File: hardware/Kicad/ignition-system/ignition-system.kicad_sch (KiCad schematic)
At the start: 27 parts, among them J1 Screw_Terminal_01x02, SW1 SW_Push, SW2 SW_SPDT

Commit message: fix: socket ra02 con gnd de bordes y ntc al temp
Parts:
- added TH1: NTC 10k B3950, Connector_JST:JST_PH_S2B-PH-K_1x02_P2.00mm_Horizontal, symbol Device:Thermistor_NTC
- SW1: footprint Connector_PinHeader_2.54mm:PinHeader_1x02_P2.54mm_Vertical -> Connector_JST:JST_PH_S2B-PH-K_1x02_P2.00mm_Horizontal
- renumbered LORA2-Sx1278 to LORA-Sx1278(A)1, LORA1-Sx1278 to LORA-Sx1278(B)1
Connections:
- net GND: now also LORA-Sx1278(A)1.1 (Pin_1), LORA-Sx1278(B)1.1 (Pin_1), LORA-Sx1278(B)1.8 (Pin_8), TH1.2; no longer ModuloDeCarga1.1 (TEMP)
- new net: ModuloDeCarga1.1 (TEMP), TH1.1
- no-connect marks 24 -> 21

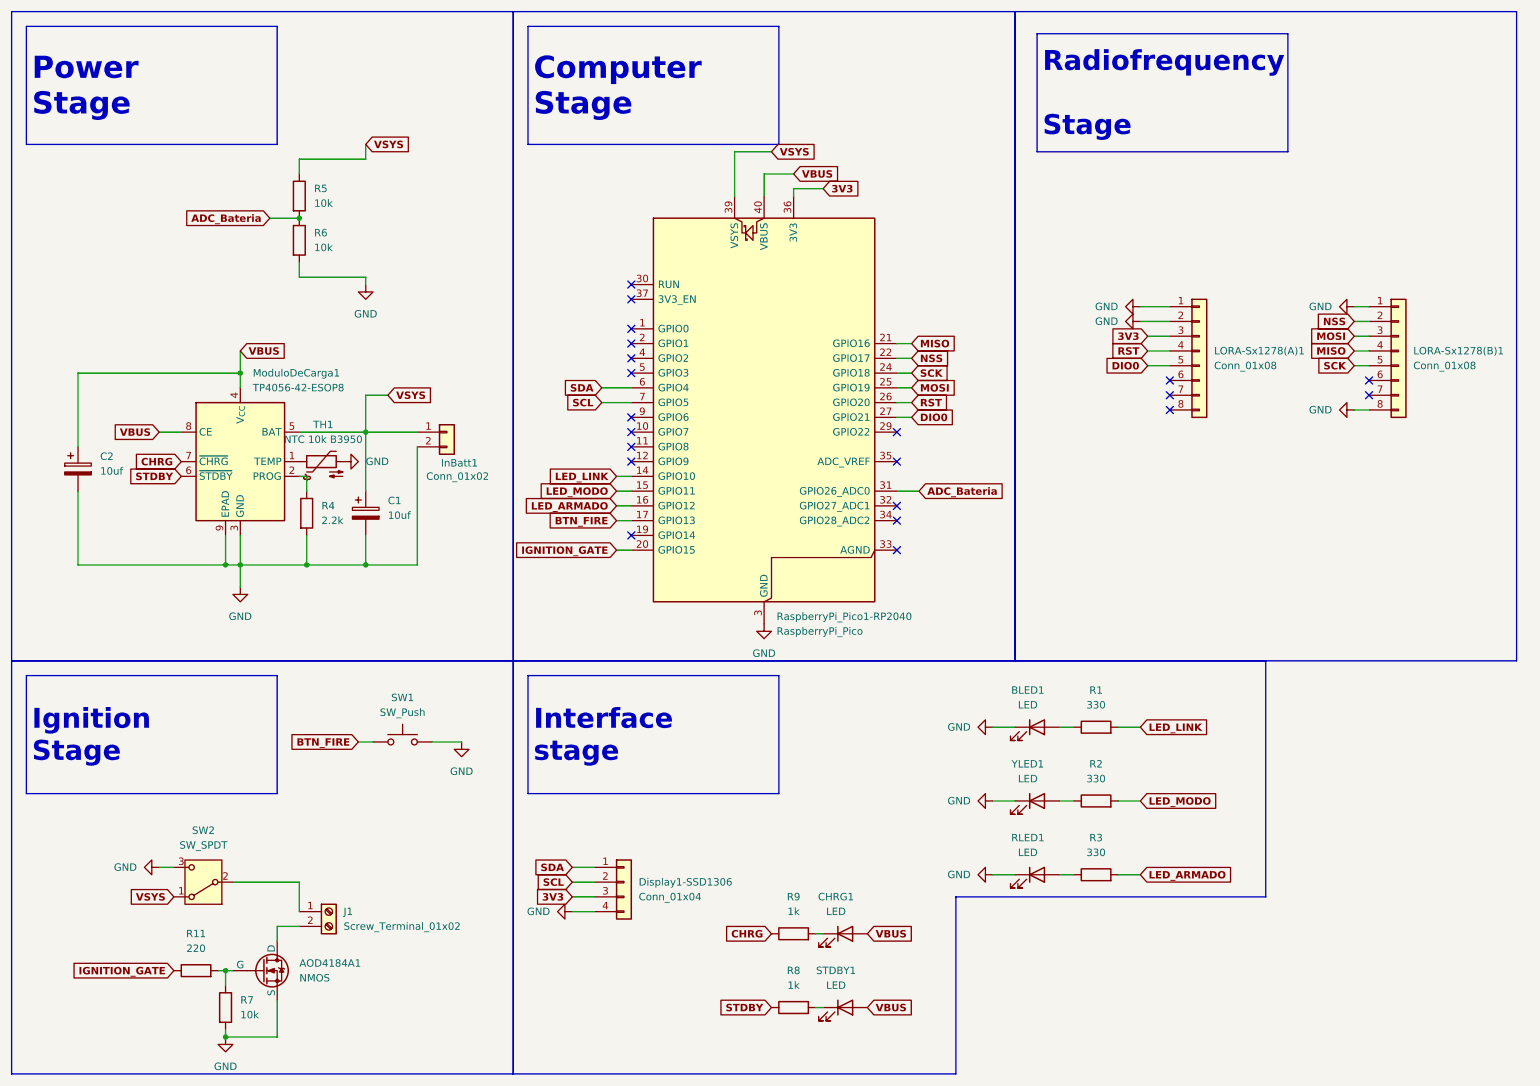
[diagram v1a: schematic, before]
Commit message: feat: sw3 en consumo, tp4056 fijo a bateria, pwr flag de v
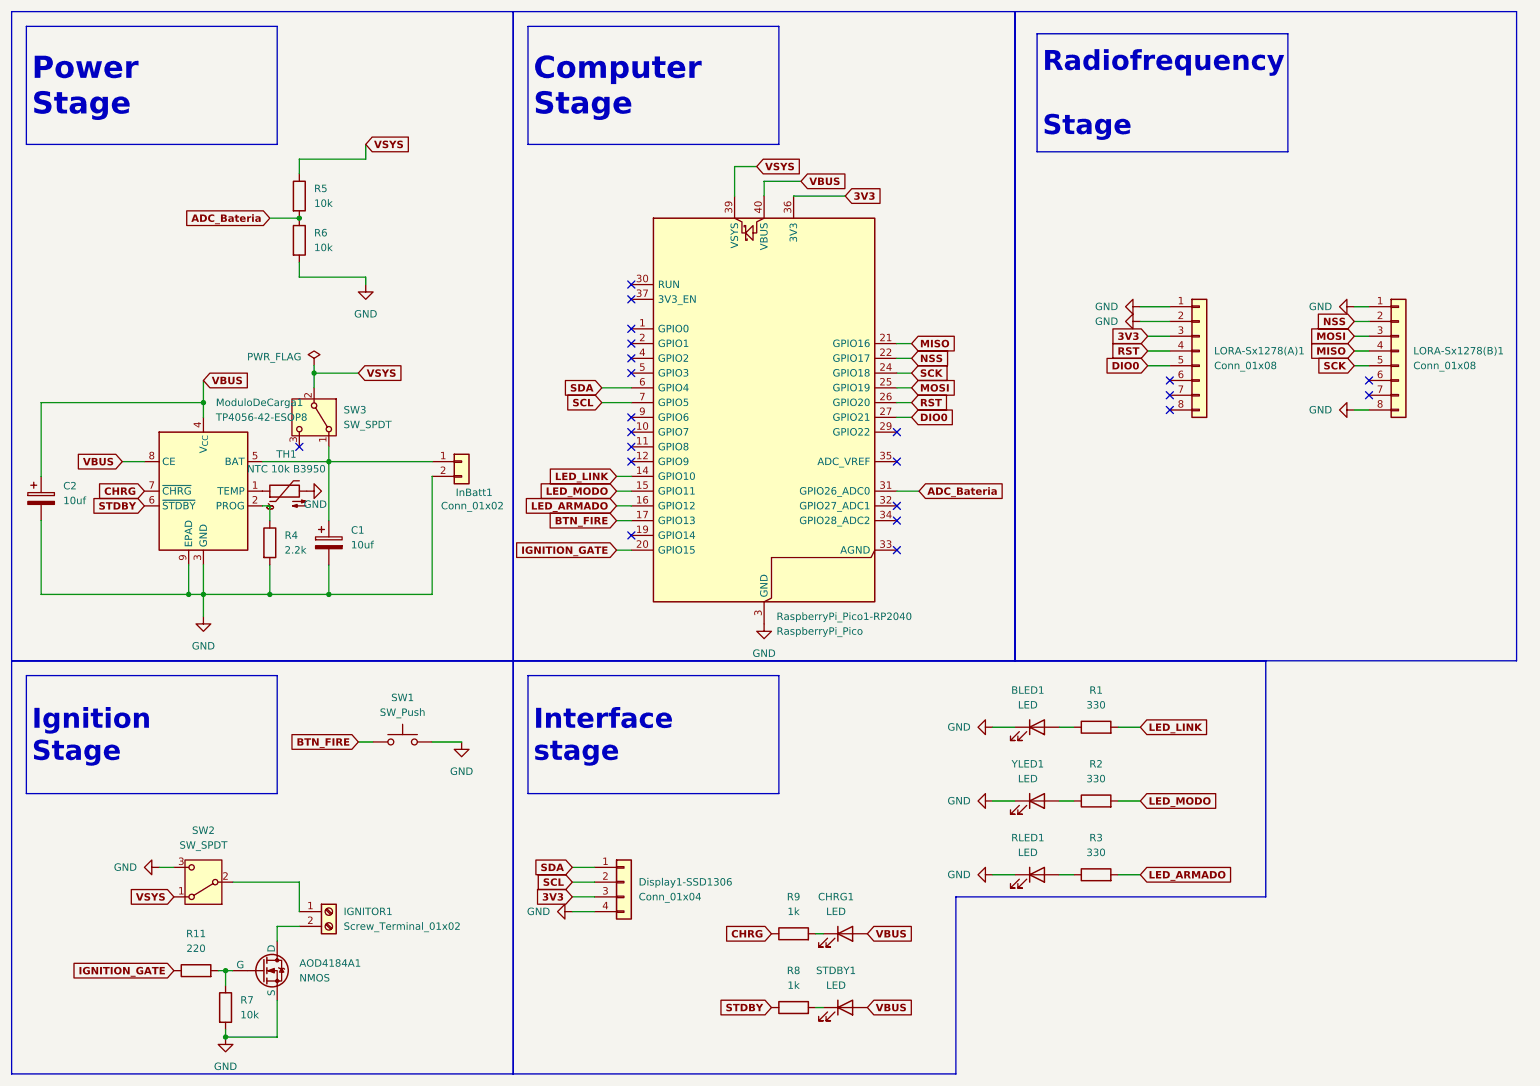
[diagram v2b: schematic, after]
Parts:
- added SW3: SW_SPDT, Button_Switch_THT:SW_E-Switch_EG1224_SPDT_Angled, symbol Switch:SW_SPDT
- renumbered J1 to IGNITOR1
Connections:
- net VSYS: now also SW3.2 (B); no longer C1.1, InBatt1.1 (Pin_1), ModuloDeCarga1.5 (BAT)
- new net: C1.1, InBatt1.1 (Pin_1), ModuloDeCarga1.5 (BAT), SW3.1 (A)
- no-connect marks 21 -> 22
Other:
- moved on the sheet: C1, C2, InBatt1, ModuloDeCarga1, R4, TH1
